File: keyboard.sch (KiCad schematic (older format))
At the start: 18 parts, among them IC30 74LS244_Split, IC35 8255A, IC52 74LS04, IC53 74LS07, IC54 74LS74, IC66 74LS322, J2 KEYBOARD, SW1 SW_DIP_x08

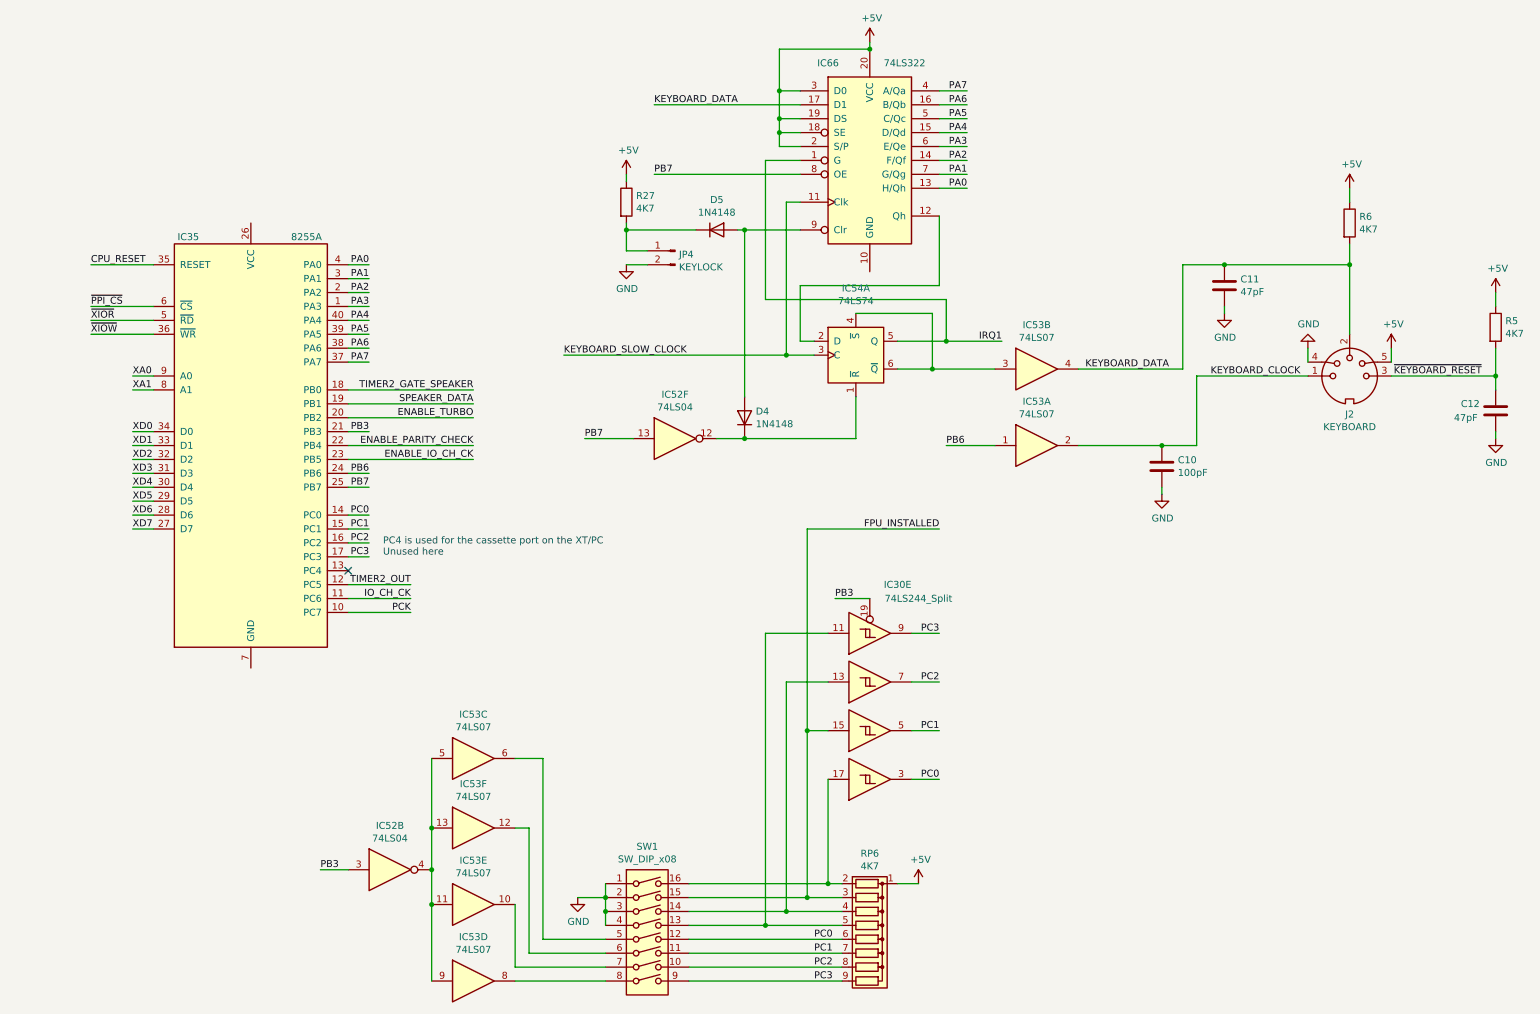
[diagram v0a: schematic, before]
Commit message: Tidy up and map all signals
This fixes up the schematic to:
 - Look presentable
 - Fix all labels connecting sheets
 - Tidy up all loose ends by either inspecting the PCB under
    magnification, measuring with an oscillosope or buzzing
    out with a meter
 - Pass ERC (with 1 exception due to incorrect circuitry around
    pin 33 on the FPU (~RQ~/~GT1~)
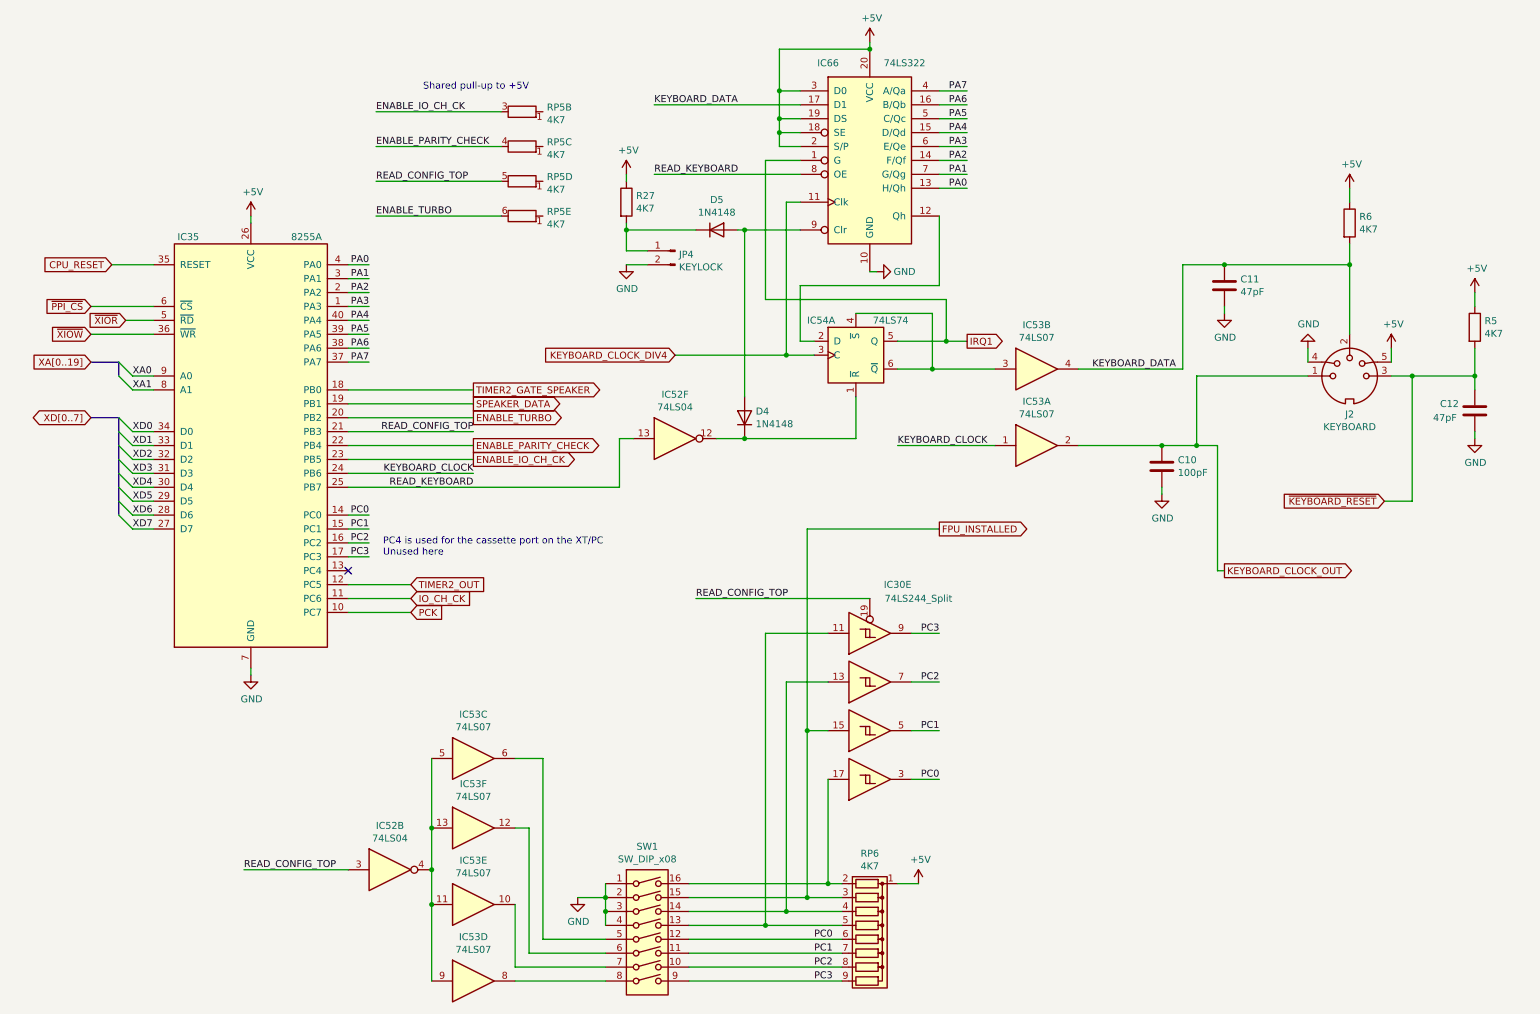
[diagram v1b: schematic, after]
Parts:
- added RP5: 4K7, Resistor_THT:R_Array_SIP9, symbol Device:R_Network08_Split
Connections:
- net PB6 is gone; now on net KEYBOARD_CLOCK: IC35.24 (PB6), IC53.1
- net +5V: now also IC35.26 (VCC)
- net ENABLE_IO_CH_CK: now also RP5.3 (R2.2)
- net ENABLE_PARITY_CHECK: now also RP5.4 (R3.2)
- net ENABLE_TURBO: now also RP5.6 (R5.2)
- net GND: now also IC35.7 (GND), IC66.10 (GND)
- net KEYBOARD_CLOCK: no longer C10.1, IC53.2, J2.1
- net KEYBOARD_SLOW_CLOCK renamed KEYBOARD_CLOCK_DIV4
- net PB3 renamed READ_CONFIG_TOP
- net READ_CONFIG_TOP: now also RP5.5 (R4.2)
- net PB7 renamed READ_KEYBOARD
- new net KEYBOARD_CLOCK_OUT: C10.1, IC53.2, J2.1
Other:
- note added: "Shared pull-up to +5V"
- moved on the sheet: C12, R5
